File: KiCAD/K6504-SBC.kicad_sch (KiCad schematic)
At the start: 40 parts, among them J1 Barrel_Jack_Switch, SW1 POWER_SW, SW2 RESET SW, U1 R6504P, U3 R6532, U4 74LS32, U5 74LS02, U6 HM62256BLP, U7 27C256, U8 74LS00, U9 74LS145, X1 1MHz

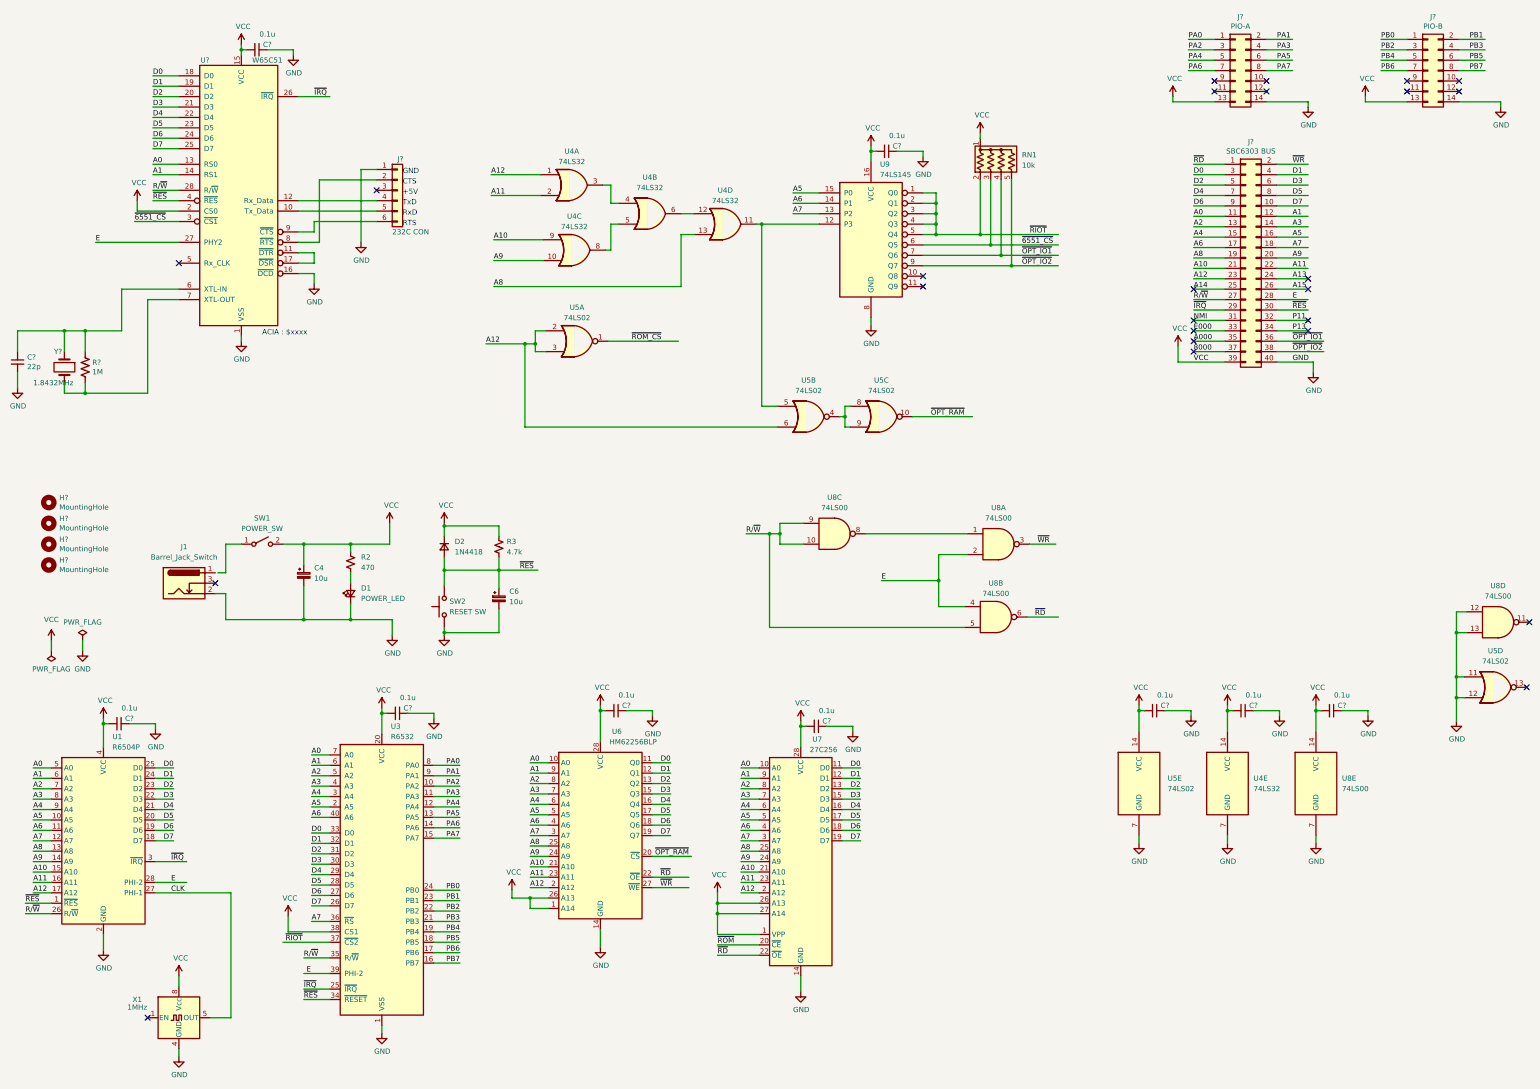
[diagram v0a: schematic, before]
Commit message: メモリーマップ見直し & 回路図見直し
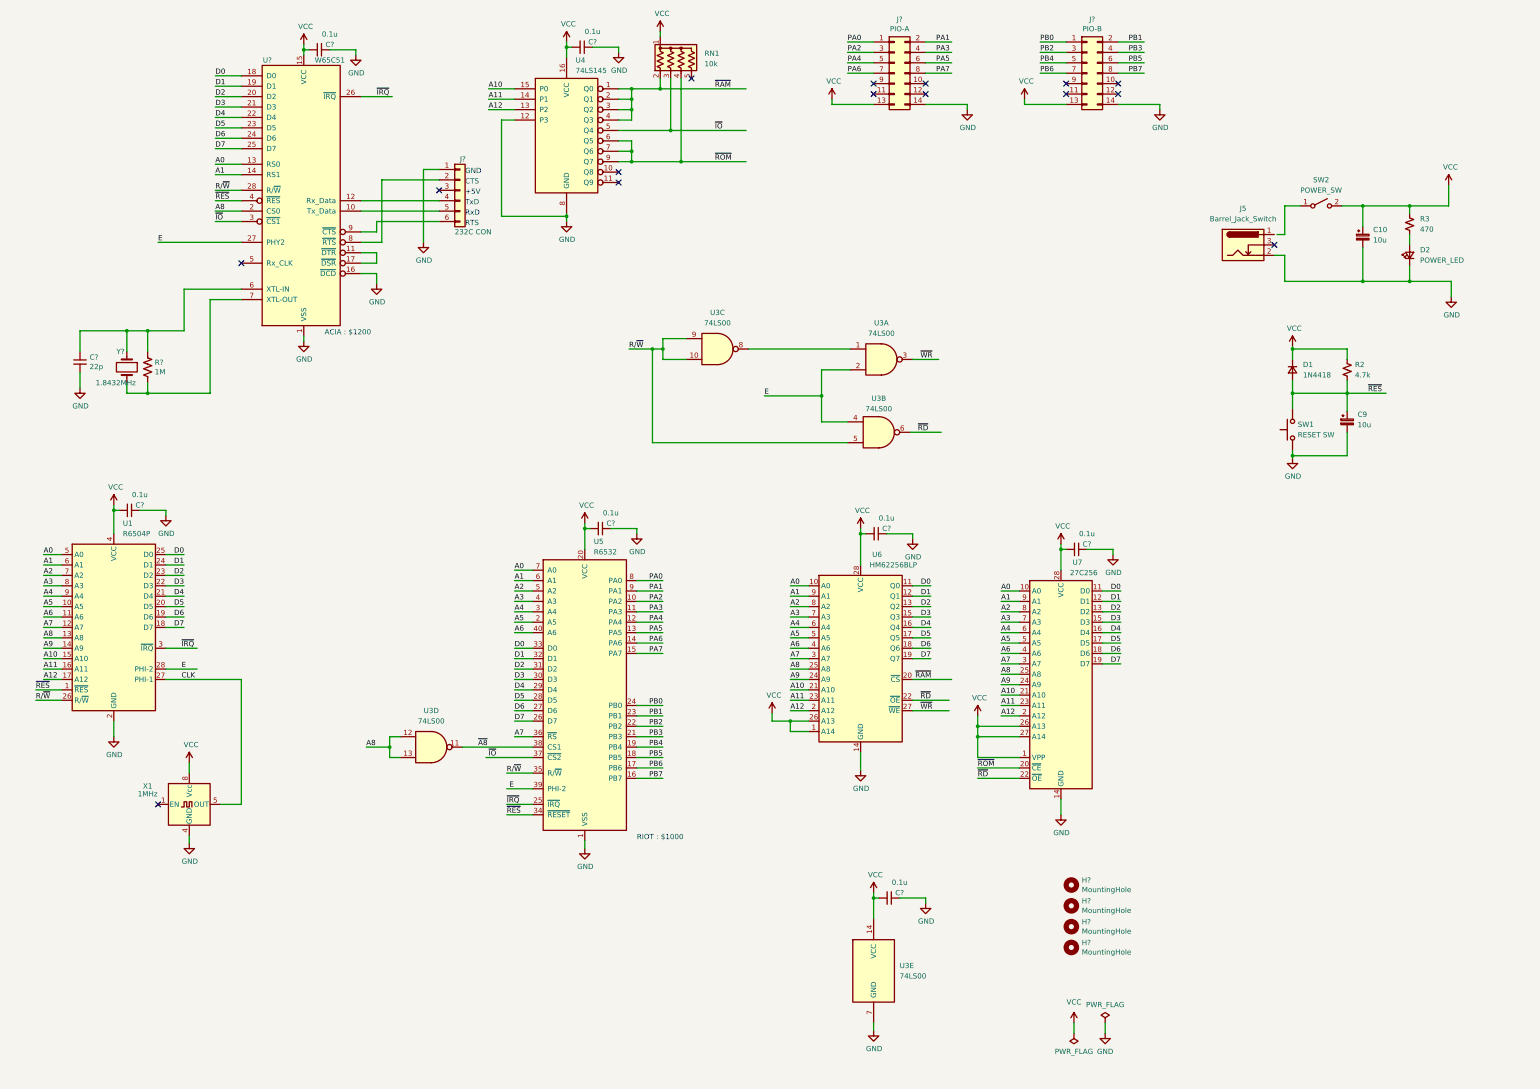
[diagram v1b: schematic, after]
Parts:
- removed C? (x2): 0.1u, Capacitor_THT:C_Disc_D3.0mm_W1.6mm_P2.50mm, symbol Device:C_Small
- removed J?: SBC6303 BUS, Connector_PinHeader_2.54mm:PinHeader_2x20_P2.54mm_Horizontal, symbol Connector_Generic:Conn_02x20_Odd_Even
- removed U4: 74LS32, symbol 74xx:74LS32
- removed U5: 74LS02, symbol 74xx:74LS02
- renumbered C4 to C10, C6 to C9, D2 to D1, D1 to D2, J1 to J5, R3 to R2, R2 to R3, SW2 to SW1, SW1 to SW2, U8 to U3, U9 to U4, U3 to U5
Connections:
- net ~{OPT_IO1} is gone; now on net ~{ROM}: RN1.4 (R3), U4.7 (Q6)
- net A10: now also U4.15 (P0)
- net A11: now also U4.14 (P1)
- net A12: now also U4.13 (P2)
- net A5: no longer U4.15 (P0)
- net A6: no longer U4.14 (P1)
- net A7: no longer U4.13 (P2)
- net A8: now also U3.12, U3.13, U?.2 (CS0)
- net GND: now also U4.12 (P3); no longer U3.12, U3.13
- net VCC: no longer U5.38 (CS1), U?.2 (CS0)
- net ~{ROM}: now also U4.6 (Q5), U4.9 (Q7)
- net ~{A8}: now reaches U3.11
- net ~{A8}: now also U5.38 (CS1)
- net ~{6551_CS} renamed ~{IO}
- net ~{IO}: now also U4.5 (Q4), U5.37 (~{CS2}); no longer U4.6 (Q5)
- net ~{OPT_IO2}: no longer names the net of RN1.5 (R4)
- net ~{OPT_IO2}: no longer U4.9 (Q7)
- net ~{OPT_RAM} renamed ~{RAM}
- net ~{RAM}: now also RN1.2 (R1), U4.1 (Q0), U4.2 (Q1), U4.3 (Q2), U4.4 (Q3)
- removed net ~{RIOT}: RN1.2 (R1), U4.1 (Q0), U4.2 (Q1), U4.3 (Q2), U4.4 (Q3), U4.5 (Q4), U5.37 (~{CS2})
- no-connect marks 25 -> 15
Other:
- note added: "ACIA : $1200"
- note added: "RIOT : $1000"
- note removed: "ACIA : $xxxx"
- moved on the sheet: C10, C9, C?, D1, D2, H?, J5, J?, R2, R3, R?, SW1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

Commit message: 回路図見直し
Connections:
- net A8: no longer U3.12, U3.13, U?.2 (CS0)
- net A9: now also U3.12, U3.13, U?.2 (CS0)
- net ~{A8} renamed ~{A9}
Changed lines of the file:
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@@
     (effects (font (size 1.27 1.27)) (justify left bottom))
   )
-  (label "A8" (at 104.14 199.39 0) (fields_autoplaced)
+  (label "A9" (at 104.14 199.39 0) (fields_autoplaced)
     (effects (font (size 1.27 1.27)) (justify left bottom))
   )
@@
     (effects (font (size 1.27 1.27)) (justify left bottom))
   )
-  (label "A8" (at 67.31 68.58 0) (fields_autoplaced)
+  (label "A9" (at 67.31 68.58 0) (fields_autoplaced)
     (effects (font (size 1.27 1.27)) (justify left bottom))
   )
@@
     (effects (font (size 1.27 1.27)) (justify right bottom))
   )
-  (label "~{A8}" (at 131.445 199.39 0) (fields_autoplaced)
-    (effects (font (size 1.27 1.27)) (justify left bottom))
-  )
+  (label "~{A9}" (at 131.445 199.39 0) (fields_autoplaced)
+    (effects (font (size 1.27 1.27)) (justify left bottom))
+  )

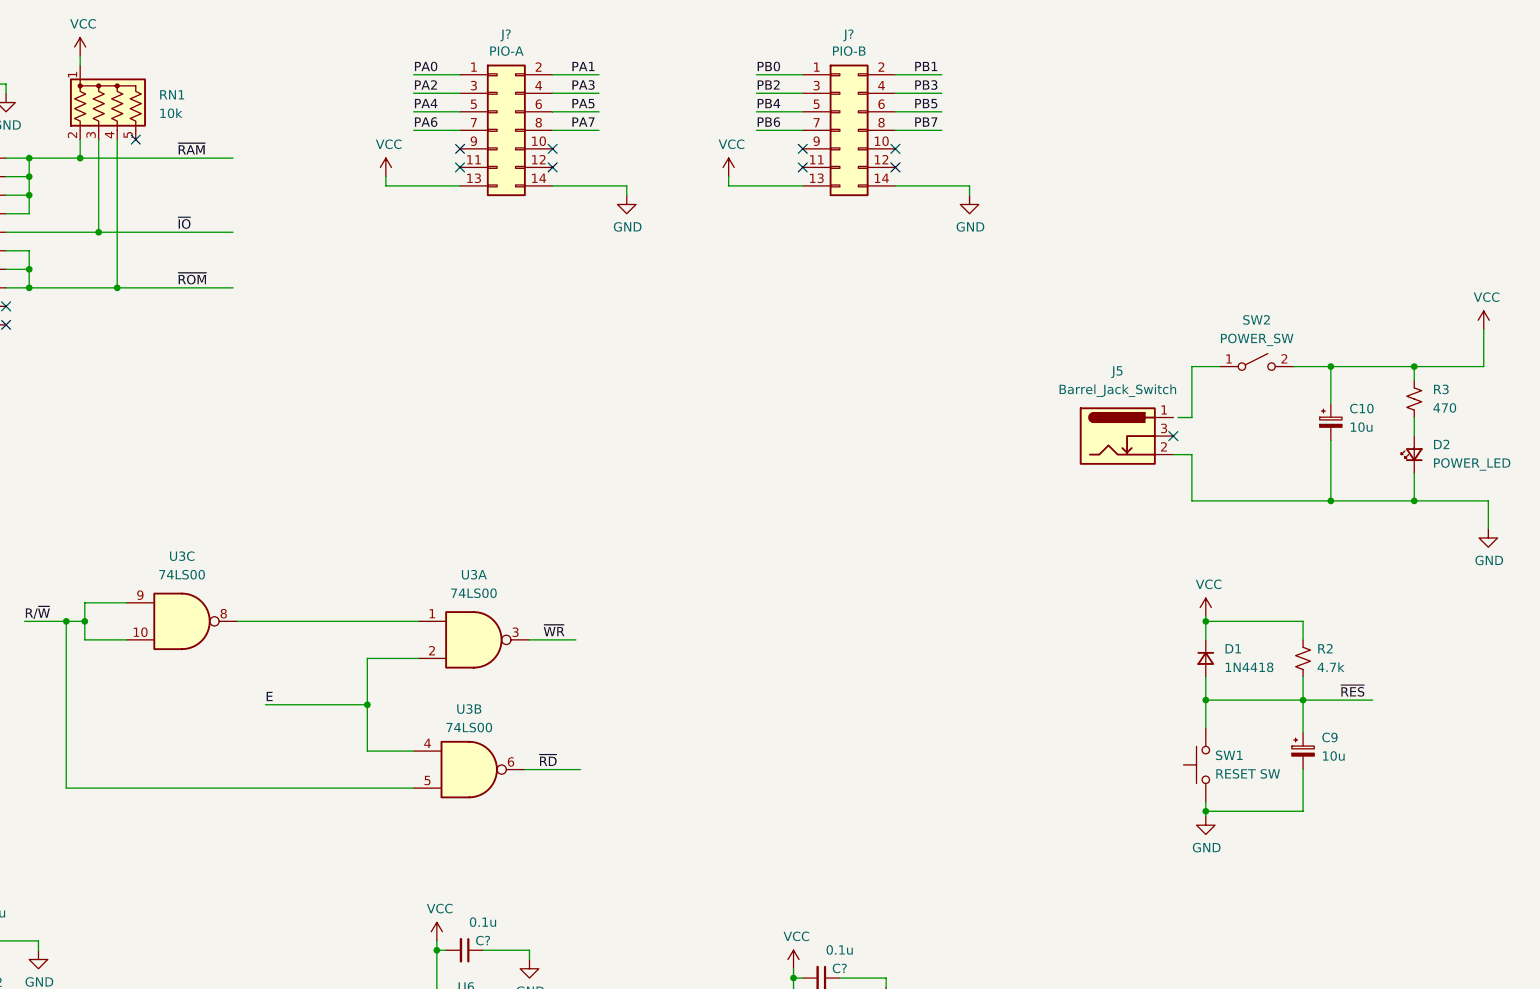
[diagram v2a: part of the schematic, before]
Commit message: 回路図  : R6404シンボル間違い修正、IRQプルアップ忘れ修正
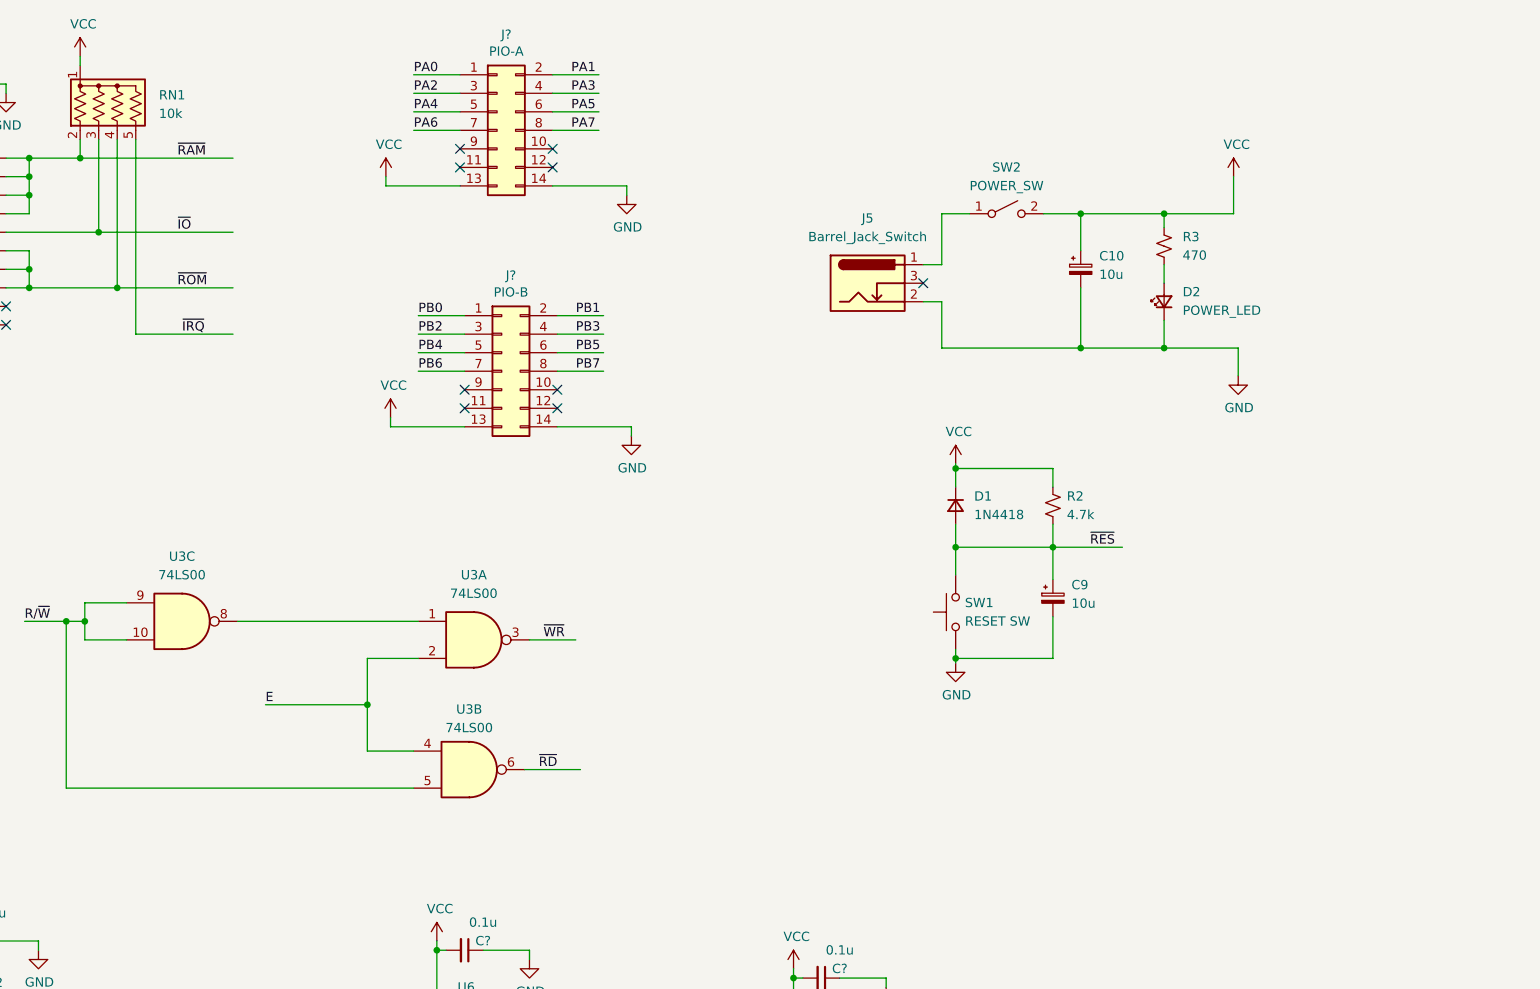
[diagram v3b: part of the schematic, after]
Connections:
- net ~{IRQ}: now also RN1.5 (R4)
- net at J5.1: now also SW2.1 (A)
- no-connect marks 15 -> 14
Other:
- moved on the sheet: C10, C9, D1, D2, J5, J?, R2, R3, SW1, SW2
